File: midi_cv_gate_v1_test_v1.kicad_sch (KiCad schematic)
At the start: 40 parts, among them J1 Conn_02x05_Odd_Even, J2 Conn_01x20, J3 Conn_01x08, J4 Conn_01x20, U1 LM7805_TO220, U2 ARDUINO_PRO_MINI_custom_2

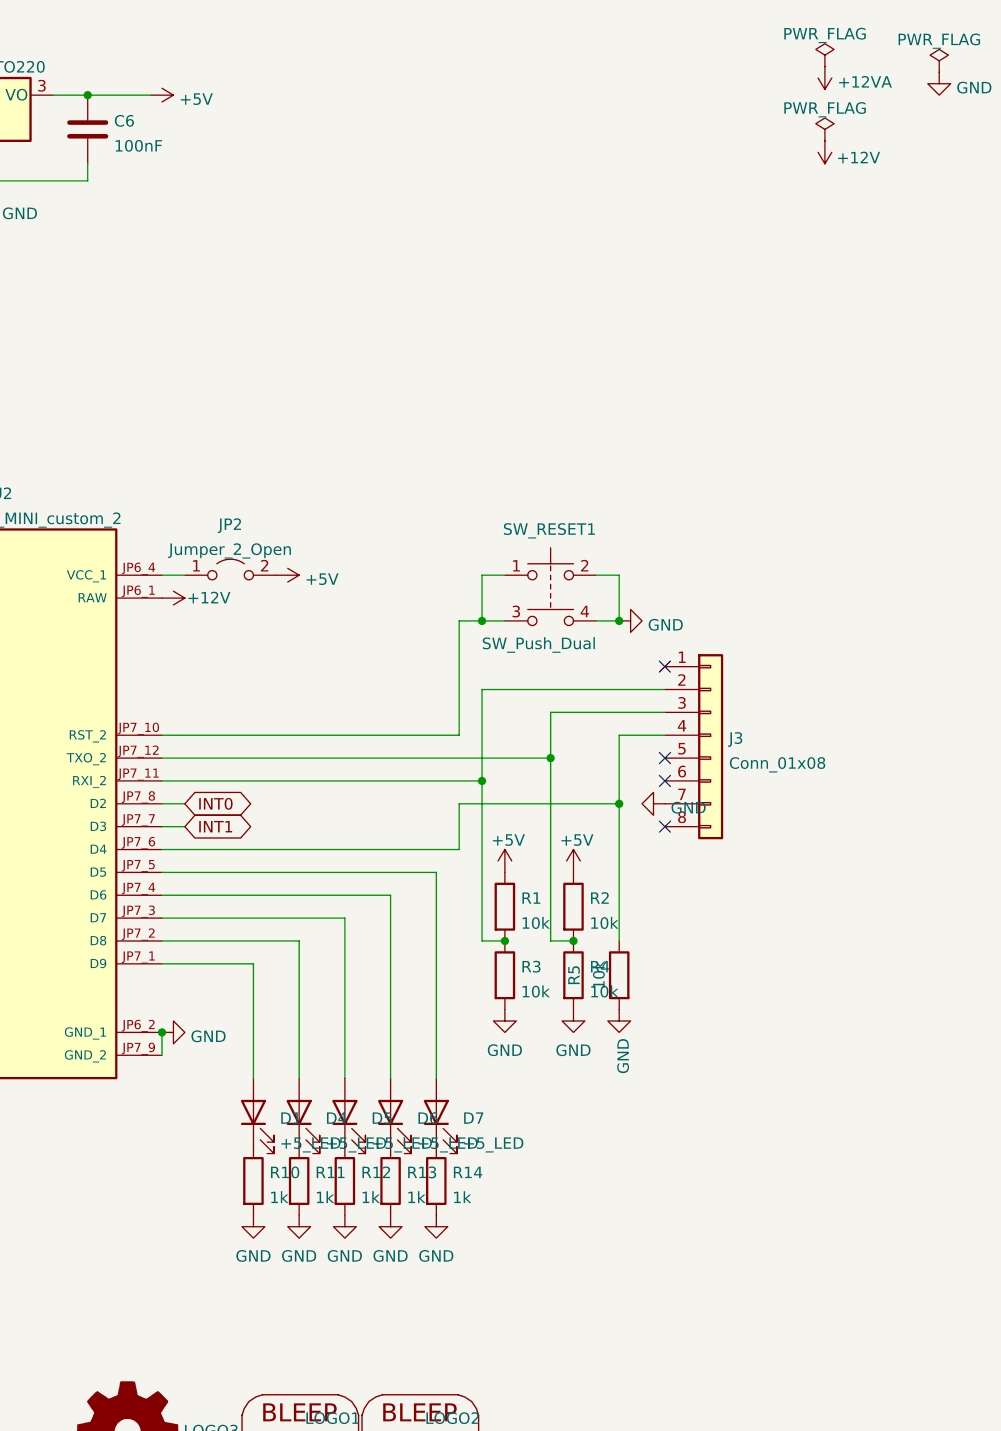
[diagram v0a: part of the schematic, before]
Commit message: Component positions first draft
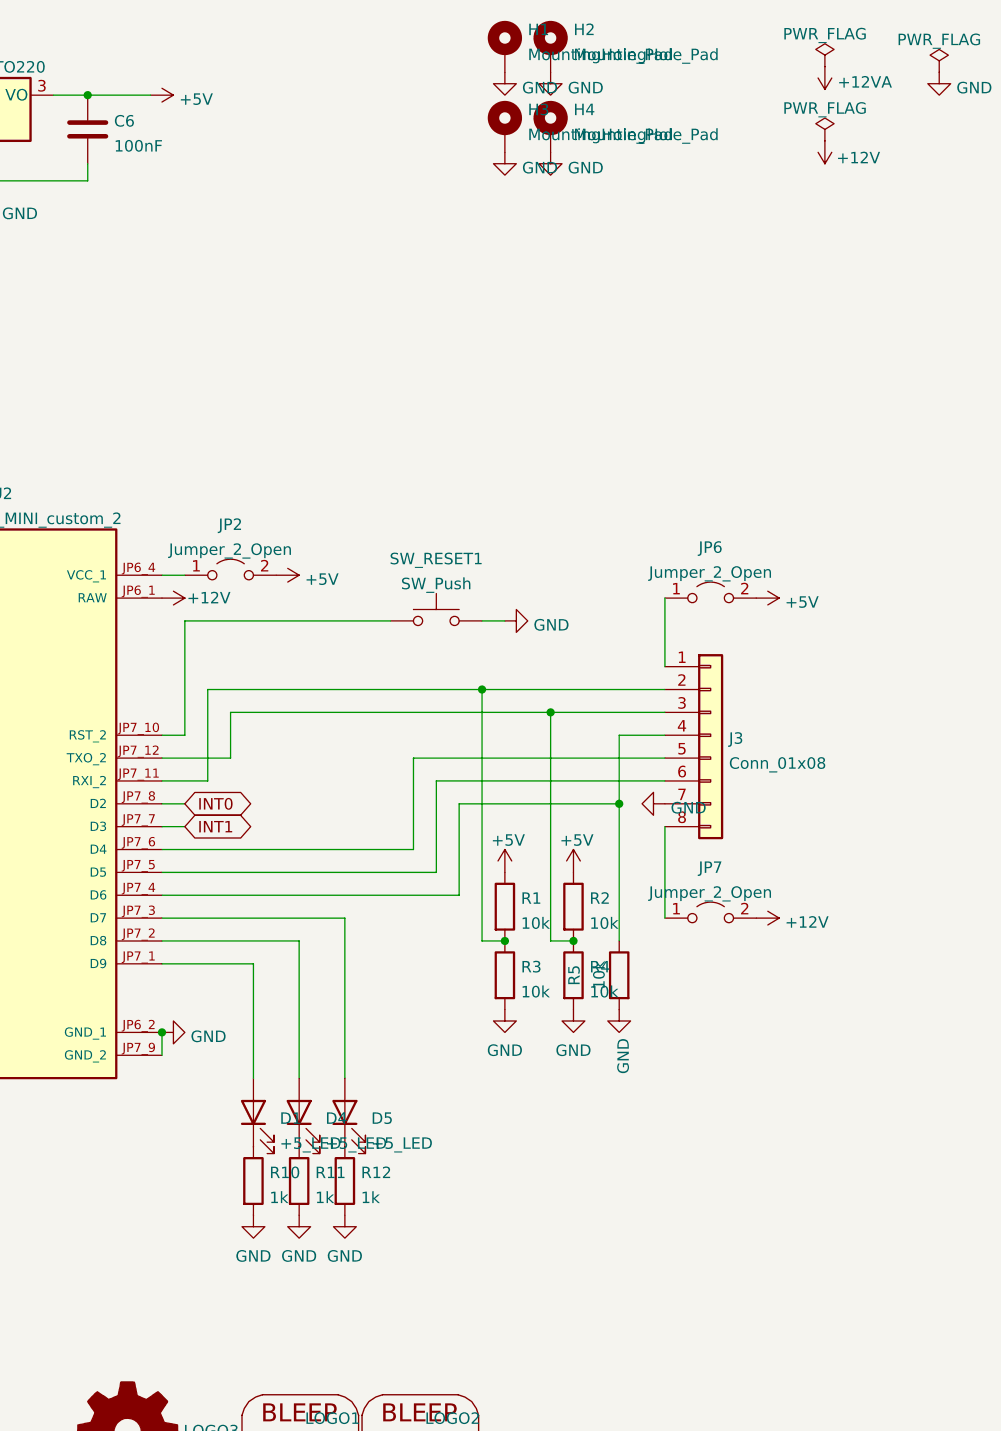
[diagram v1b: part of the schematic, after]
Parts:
- removed D6, D7: +5_LED, LED_THT:LED_D3.0mm, symbol Device:LED
- removed R13, R14: 1k, Resistor_SMD:R_1206_3216Metric_Pad1.30x1.75mm_HandSolder, symbol Device:R
- removed SW_RESET1: SW_Push_Dual, Button_Switch_THT:SW_PUSH_6mm_H5mm, symbol Switch:SW_Push_Dual
- added H1, H2, H3, H4: MountingHole_Pad, MountingHole:MountingHole_3.2mm_M3_ISO7380_Pad_TopBottom, symbol Mechanical:MountingHole_Pad
- added JP6, JP7: Jumper_2_Open, Jumper:SolderJumper-2_P1.3mm_Open_Pad1.0x1.5mm, symbol Jumper:Jumper_2_Open
- added SW_RESET1: SW_Push, Button_Switch_THT:SW_PUSH_6mm_H5mm, symbol Switch:SW_Push
- U1: footprint Package_TO_SOT_THT:TO-220-3_Vertical -> Package_TO_SOT_THT:TO-220-3_Horizontal_TabDown
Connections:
- net +12V: now also JP7.2 (B)
- net +5V: now also JP6.2 (B)
- net GND: now also H1.1, H2.1, H3.1, H4.1, SW_RESET1.2
- net at U2.JP7_10 (RST_2): now also SW_RESET1.1
- net at U2.JP7_4 (D6): now also J3.4 (Pin_4), R5.1
- net at U2.JP7_5 (D5): now also J3.6 (Pin_6)
- net at J3.1 (Pin_1): now also JP6.1 (A)
- net at J3.5 (Pin_5): now also U2.JP7_6 (D4)
- net at J3.8 (Pin_8): now also JP7.1 (A)
- no-connect marks 9 -> 5

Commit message: Geographic re-annotate
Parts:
- renumbered C3 to C1, C1 to C101, C4 to C2, C6 to C3, D3 to D100, D5 to D101, D4 to D102, D1 to D103, FB2 to FB100, H3 to H2, H2 to H3, J2 to J1, J1 to J101, J3 to J2, J4 to J3, JP5 to JP101, JP4 to JP2, JP6 to JP3, JP7 to JP4, JP2 to JP6, JP3 to JP7, LOGO3 to LOGO1, LOGO1 to LOGO2, LOGO2 to LOGO3, R6 to R17, R4 to R18, R2 to R19, R7 to R36, R5 to R37, R10 to R38, R11 to R41, R1 to R48, R12 to R49, R3 to R52, R9 to R66, R8 to R67, SW_RESET1 to SW_RESET100, U2 to U103, U1 to U105

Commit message: A little cleanup
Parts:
- D101: value +5_LED -> LED3
- D102: value +5_LED -> LED2
- D103: value +5_LED -> LED1

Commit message: Resync pcb and schematic
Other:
- title: (none) -> MIDI CV GATE Test Fixture
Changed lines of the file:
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@@
   (paper "A4")
   (title_block
+    (title "MIDI CV GATE Test Fixture")
+    (date "2022-10-15")
+    (rev "1.0")
     (company "RobotDialogs")
   )

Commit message: Component updates and rework info v1
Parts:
- R18, R52: value 10k -> DNU
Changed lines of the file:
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@@
   (symbol (lib_id "Device:R") (at 233.68 123.19 0) (unit 1)
     (in_bom yes) (on_board yes)
-    (property "Reference" "R18" (id 0) (at 236.855 125.095 90)
-      (effects (font (size 1.27 1.27)) (justify left))
-    )
-    (property "Value" "10k" (id 1) (at 233.68 124.46 90)
+    (property "Reference" "R18" (id 0) (at 231.14 125.095 90)
+      (effects (font (size 1.27 1.27)) (justify left))
+    )
+    (property "Value" "DNU" (id 1) (at 233.68 124.46 90)
       (effects (font (size 1.27 1.27)) (justify left))
     )
@@
   (symbol (lib_id "Device:R") (at 226.06 123.19 0) (unit 1)
     (in_bom yes) (on_board yes)
-    (property "Reference" "R52" (id 0) (at 224.155 125.095 90)
-      (effects (font (size 1.27 1.27)) (justify left))
-    )
-    (property "Value" "10k" (id 1) (at 226.06 124.46 90)
+    (property "Reference" "R52" (id 0) (at 223.52 125.095 90)
+      (effects (font (size 1.27 1.27)) (justify left))
+    )
+    (property "Value" "DNU" (id 1) (at 226.06 124.46 90)
       (effects (font (size 1.27 1.27)) (justify left))
     )
@@
   (symbol (lib_id "Device:R") (at 238.76 123.19 0) (mirror y) (unit 1)
     (in_bom yes) (on_board yes)
-    (property "Reference" "R37" (id 0) (at 231.775 123.19 90))
+    (property "Reference" "R37" (id 0) (at 241.3 123.19 90))
     (property "Value" "10k" (id 1) (at 238.76 123.825 90))
     (property "Footprint" "Resistor_SMD:R_1206_3216Metric_Pad1.30x1.75mm_HandSolder" (id 2) (at 240.538 123.19 90)
@@
     )
     (path "/3e363310-fb12-4968-9a63-66d2022e0b03"
-      (reference "R18") (unit 1) (value "10k") (footprint "Resistor_SMD:R_1206_3216Metric_Pad1.30x1.75mm_HandSolder")
+      (reference "R18") (unit 1) (value "DNU") (footprint "Resistor_SMD:R_1206_3216Metric_Pad1.30x1.75mm_HandSolder")
     )
     (path "/ffdead50-1655-4a92-997a-6d10ec794470"
@@
     )
     (path "/2fc744ec-e757-4bd0-a4d4-22a6e3206a1e/00772a9c-368a-41f2-819b-1f5e72bc8bc0"
-      (reference "R40") (unit 1) (value "10k") (footprint "Resistor_SMD:R_1206_3216Metric_Pad1.30x1.75mm_HandSolder")
+      (reference "R40") (unit 1) (value "DNU") (footprint "Resistor_SMD:R_1206_3216Metric_Pad1.30x1.75mm_HandSolder")
     )
     (path "/931d5a76-831a-47b9-98ba-09495b972af5"
@@
     )
     (path "/2fc744ec-e757-4bd0-a4d4-22a6e3206a1e/f0dc5a3d-ce17-4f52-a737-e262bb4d9d95"
-      (reference "R42") (unit 1) (value "10k") (footprint "Resistor_SMD:R_1206_3216Metric_Pad1.30x1.75mm_HandSolder")
+      (reference "R42") (unit 1) (value "DNU") (footprint "Resistor_SMD:R_1206_3216Metric_Pad1.30x1.75mm_HandSolder")
     )
     (path "/2fc744ec-e757-4bd0-a4d4-22a6e3206a1e/328e09e5-7df7-4fea-ac05-269c471ea2ea"
@@
     )
     (path "/2fc744ec-e757-4bd0-a4d4-22a6e3206a1e/7bcc873c-292e-44c6-9f52-3d63ec3d0a99"
-      (reference "R44") (unit 1) (value "10k") (footprint "Resistor_SMD:R_1206_3216Metric_Pad1.30x1.75mm_HandSolder")
+      (reference "R44") (unit 1) (value "DNU") (footprint "Resistor_SMD:R_1206_3216Metric_Pad1.30x1.75mm_HandSolder")
     )
     (path "/2fc744ec-e757-4bd0-a4d4-22a6e3206a1e/40ab2d47-2e63-4993-9ca6-57bb1b6b4a47"
@@
     )
     (path "/2fc744ec-e757-4bd0-a4d4-22a6e3206a1e/b1c05788-6976-4983-a75a-c20e73db95e1"
-      (reference "R46") (unit 1) (value "10k") (footprint "Resistor_SMD:R_1206_3216Metric_Pad1.30x1.75mm_HandSolder")
+      (reference "R46") (unit 1) (value "DNU") (footprint "Resistor_SMD:R_1206_3216Metric_Pad1.30x1.75mm_HandSolder")
     )
     (path "/2fc744ec-e757-4bd0-a4d4-22a6e3206a1e/441cc469-5893-4d4c-9b57-4bd25cdbc966"
@@
     )
     (path "/7fd56235-4d61-4fcf-8c83-c3cd882749e6"
-      (reference "R52") (unit 1) (value "10k") (footprint "Resistor_SMD:R_1206_3216Metric_Pad1.30x1.75mm_HandSolder")
+      (reference "R52") (unit 1) (value "DNU") (footprint "Resistor_SMD:R_1206_3216Metric_Pad1.30x1.75mm_HandSolder")
     )
     (path "/c79151ae-7c21-48f7-9574-98b556cec7bb/4aa10692-7c5b-4700-b6fc-d529e4e79dc6"
@@
     )
     (path "/2fc744ec-e757-4bd0-a4d4-22a6e3206a1e/c15882a8-42c2-4101-8327-e6fd9dbe8187"
-      (reference "R54") (unit 1) (value "10k") (footprint "Resistor_SMD:R_1206_3216Metric_Pad1.30x1.75mm_HandSolder")
+      (reference "R54") (unit 1) (value "DNU") (footprint "Resistor_SMD:R_1206_3216Metric_Pad1.30x1.75mm_HandSolder")
     )
     (path "/2fc744ec-e757-4bd0-a4d4-22a6e3206a1e/afbd5ea6-4641-452e-ba62-aa4985468739"
-      (reference "R55") (unit 1) (value "10k") (footprint "Resistor_SMD:R_1206_3216Metric_Pad1.30x1.75mm_HandSolder")
+      (reference "R55") (unit 1) (value "DNU") (footprint "Resistor_SMD:R_1206_3216Metric_Pad1.30x1.75mm_HandSolder")
     )
     (path "/c79151ae-7c21-48f7-9574-98b556cec7bb/8d0d162b-a128-49bc-afa3-3768821a8e3d"
@@
     )
     (path "/c79151ae-7c21-48f7-9574-98b556cec7bb/5fba1d25-75d9-4d2a-aea0-b0828da156c6"
-      (reference "R57") (unit 1) (value "10k") (footprint "Resistor_SMD:R_1206_3216Metric_Pad1.30x1.75mm_HandSolder")
+      (reference "R57") (unit 1) (value "DNU") (footprint "Resistor_SMD:R_1206_3216Metric_Pad1.30x1.75mm_HandSolder")
     )
     (path "/c79151ae-7c21-48f7-9574-98b556cec7bb/82843550-a579-42bd-8571-108ad4aa954e"
-      (reference "R58") (unit 1) (value "10k") (footprint "Resistor_SMD:R_1206_3216Metric_Pad1.30x1.75mm_HandSolder")
+      (reference "R58") (unit 1) (value "DNU") (footprint "Resistor_SMD:R_1206_3216Metric_Pad1.30x1.75mm_HandSolder")
     )
     (path "/c79151ae-7c21-48f7-9574-98b556cec7bb/e62a01e5-9249-49cf-b731-87e766ea40ad"
-      (reference "R59") (unit 1) (value "10k") (footprint "Resistor_SMD:R_1206_3216Metric_Pad1.30x1.75mm_HandSolder")
+      (reference "R59") (unit 1) (value "DNU") (footprint "Resistor_SMD:R_1206_3216Metric_Pad1.30x1.75mm_HandSolder")
     )
     (path "/c79151ae-7c21-48f7-9574-98b556cec7bb/570b3301-eb4a-47f8-bf7f-7ead851a5741"
@@
     )
     (path "/c79151ae-7c21-48f7-9574-98b556cec7bb/4a004c8e-fe3e-4cc7-9f3e-102c954f957a"
-      (reference "R61") (unit 1) (value "10k") (footprint "Resistor_SMD:R_1206_3216Metric_Pad1.30x1.75mm_HandSolder")
+      (reference "R61") (unit 1) (value "DNU") (footprint "Resistor_SMD:R_1206_3216Metric_Pad1.30x1.75mm_HandSolder")
     )
     (path "/c79151ae-7c21-48f7-9574-98b556cec7bb/c9a774f7-f795-4eb1-921e-897b20d1698f"
-      (reference "R62") (unit 1) (value "10k") (footprint "Resistor_SMD:R_1206_3216Metric_Pad1.30x1.75mm_HandSolder")
+      (reference "R62") (unit 1) (value "DNU") (footprint "Resistor_SMD:R_1206_3216Metric_Pad1.30x1.75mm_HandSolder")
     )
     (path "/c79151ae-7c21-48f7-9574-98b556cec7bb/fc3ee359-9b2a-4e4d-bae3-8500c0900600"
@@
     )
     (path "/c79151ae-7c21-48f7-9574-98b556cec7bb/dab6105a-5a47-44fe-895a-787d986ad9cb"
-      (reference "R64") (unit 1) (value "10k") (footprint "Resistor_SMD:R_1206_3216Metric_Pad1.30x1.75mm_HandSolder")
+      (reference "R64") (unit 1) (value "DNU") (footprint "Resistor_SMD:R_1206_3216Metric_Pad1.30x1.75mm_HandSolder")
     )
     (path "/c79151ae-7c21-48f7-9574-98b556cec7bb/eeac3616-99ae-4981-8862-874d61ec1830"
-      (reference "R65") (unit 1) (value "10k") (footprint "Resistor_SMD:R_1206_3216Metric_Pad1.30x1.75mm_HandSolder")
+      (reference "R65") (unit 1) (value "DNU") (footprint "Resistor_SMD:R_1206_3216Metric_Pad1.30x1.75mm_HandSolder")
     )
     (path "/5cb6e0fc-ab27-4d6d-893c-591de897b92b"
